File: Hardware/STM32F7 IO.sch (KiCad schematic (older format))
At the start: 28 parts, among them U16 STM32F765ZGT6

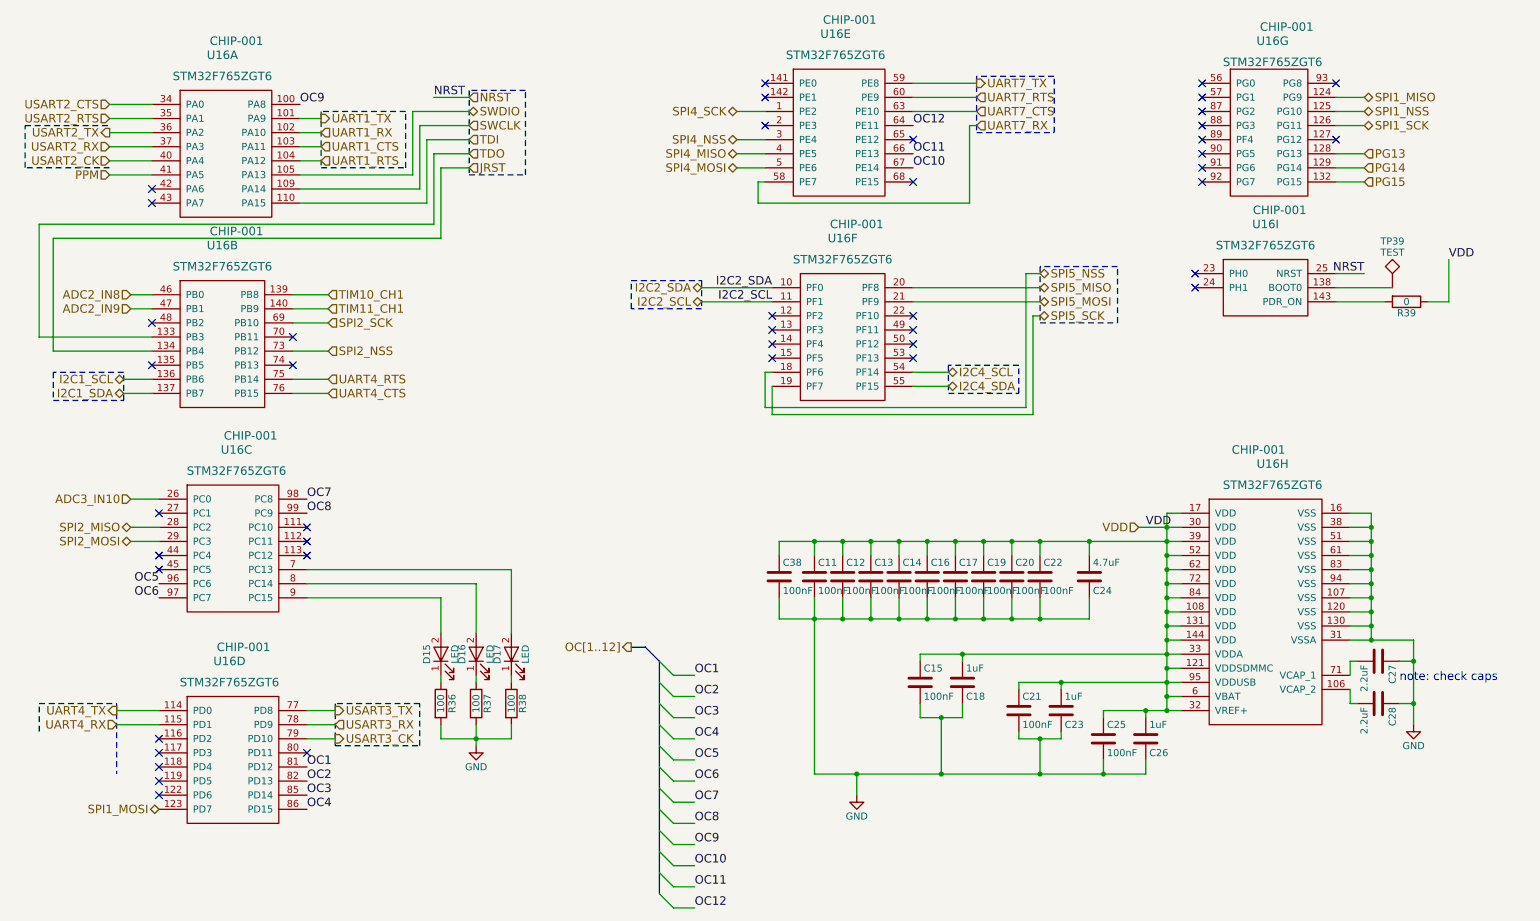
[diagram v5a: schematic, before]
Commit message: Restarted work
Removed OC and SEL busses. Still need to add clocks.
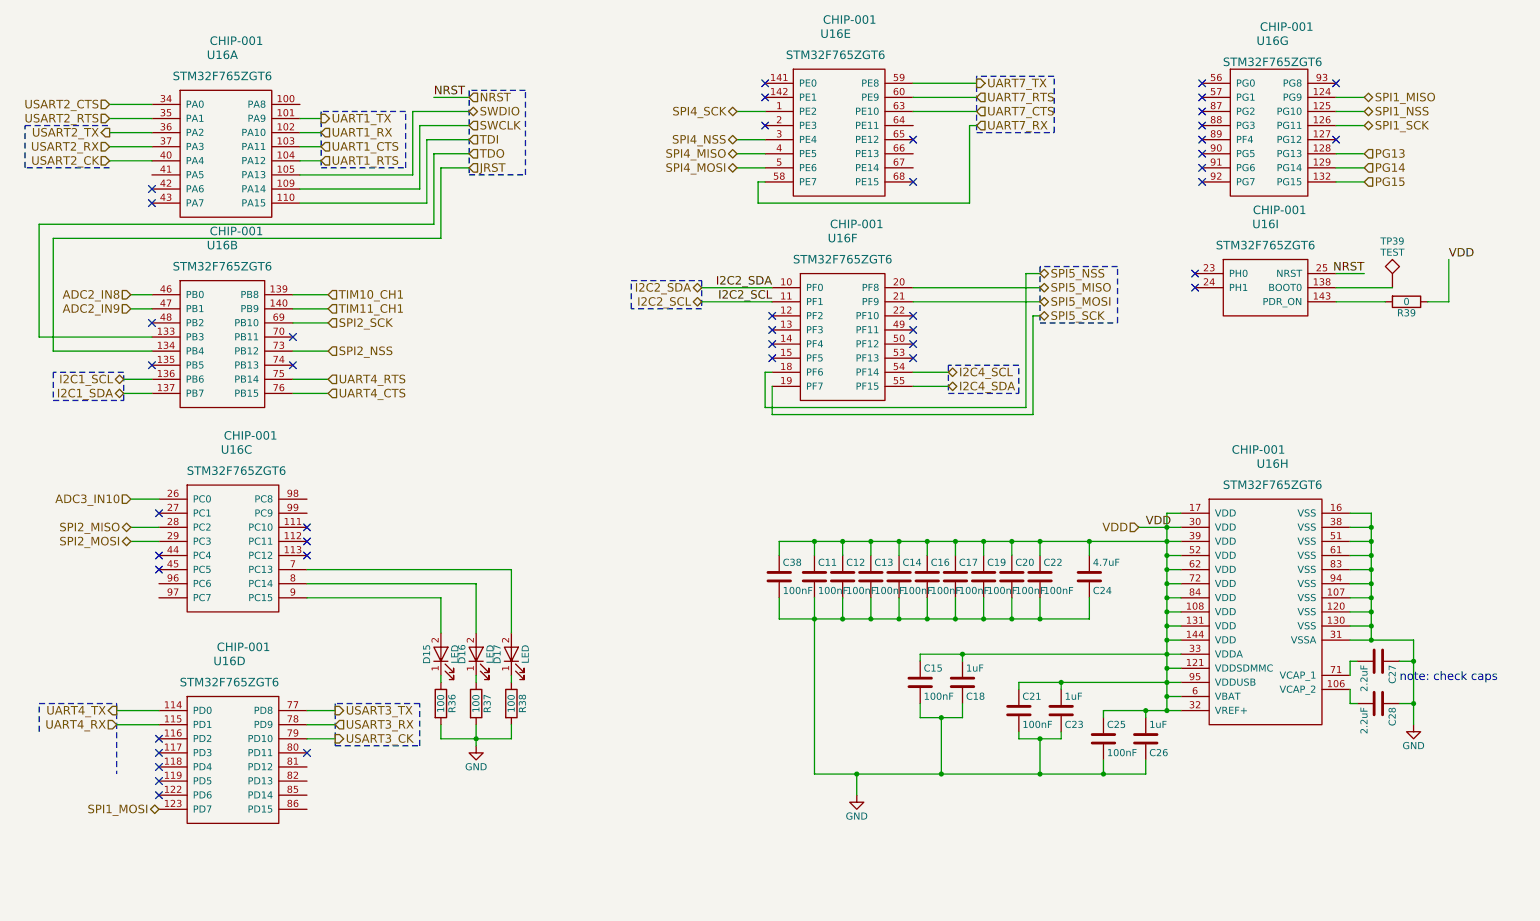
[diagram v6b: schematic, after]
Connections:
- net OC1: no longer names the net of U16.81 (PD12)
- net OC10: no longer names the net of U16.67 (PE14)
- net OC11: no longer names the net of U16.66 (PE13)
- net OC12: no longer names the net of U16.64 (PE11)
- net OC2: no longer names the net of U16.82 (PD13)
- net OC3: no longer names the net of U16.85 (PD14)
- net OC4: no longer names the net of U16.86 (PD15)
- net OC5: no longer names the net of U16.96 (PC6)
- net OC6: no longer names the net of U16.97 (PC7)
- net OC7: no longer names the net of U16.98 (PC8)
- net OC8: no longer names the net of U16.99 (PC9)
- net OC9: no longer names the net of U16.100 (PA8)
- net PPM: no longer names the net of U16.41 (PA5)
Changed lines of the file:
@@
 EESchema Schematic File Version 2
+LIBS:ZeroPilot-rescue
 LIBS:WARG
 LIBS:power
@@
 $Descr A4 11693 8268
 encoding utf-8
-Sheet 17 21
+Sheet 5 8
 Title "Autopilot Controller I/O"
 Date "2017-05-14"
@@
 Comment4 ""
 $EndDescr
-Text Label 2750 6300 0    60   ~ 0
-OC1
-Text Label 2750 6400 0    60   ~ 0
-OC2
-Text Label 2750 6500 0    60   ~ 0
-OC3
-Text Label 2750 6600 0    60   ~ 0
-OC4
-Text Label 1700 5000 2    60   ~ 0
-OC5
-Text Label 1700 5100 2    60   ~ 0
-OC6
-Text Label 2750 4400 0    60   ~ 0
-OC7
-Text Label 2700 1600 0    60   ~ 0
-OC9
-Text Label 7050 2050 0    60   ~ 0
-OC10
-Text Label 7050 1950 0    60   ~ 0
-OC11
-Text Label 7050 1750 0    60   ~ 0
-OC12
-Text HLabel 1350 2100 0    60   Input ~ 0
-PPM
-Text HLabel 5050 5450 0    60   Output ~ 0
-OC[1..12]
-Entry Wire Line
-	5250 5550 5350 5650
-Entry Wire Line
-	5250 5700 5350 5800
-Entry Wire Line
-	5250 5850 5350 5950
-Entry Wire Line
-	5250 6000 5350 6100
-Entry Wire Line
-	5250 6150 5350 6250
-Entry Wire Line
-	5250 6300 5350 6400
-Entry Wire Line
-	5250 6450 5350 6550
-Entry Wire Line
-	5250 6600 5350 6700
-Entry Wire Line
-	5250 6750 5350 6850
-Entry Wire Line
-	5250 6900 5350 7000
-Entry Wire Line
-	5250 7050 5350 7150
-Entry Wire Line
-	5250 7200 5350 7300
-Text Label 5500 7300 0    60   ~ 0
-OC12
-Text Label 5500 7150 0    60   ~ 0
-OC11
-Text Label 5500 7000 0    60   ~ 0
-OC10
-Text Label 5500 6850 0    60   ~ 0
-OC9
-Text Label 5500 6700 0    60   ~ 0
-OC8
-Text Label 5500 6550 0    60   ~ 0
-OC7
-Text Label 5500 6400 0    60   ~ 0
-OC6
-Text Label 5500 6250 0    60   ~ 0
-OC5
-Text Label 5500 6100 0    60   ~ 0
-OC4
-Text Label 5500 5950 0    60   ~ 0
-OC3
-Text Label 5500 5800 0    60   ~ 0
-OC2
-Text Label 5500 5650 0    60   ~ 0
-OC1
-Text Label 2750 4500 0    60   ~ 0
-OC8
 Text Label 10250 2800 2    60   ~ 0
 NRST
@@
 	7950 2800 7850 2800
 Wire Wire Line
-	1350 2100 1650 2100
-Wire Wire Line
 	2650 2950 2900 2950
 Wire Wire Line
@@
 Wire Wire Line
 	2700 2100 3500 2100
-Wire Wire Line
-	5350 7300 5500 7300
-Wire Wire Line
-	5350 7150 5500 7150
-Wire Wire Line
-	5350 7000 5500 7000
-Wire Wire Line
-	5350 6850 5500 6850
-Wire Wire Line
-	5350 6700 5500 6700
-Wire Wire Line
-	5350 6550 5500 6550
-Wire Wire Line
-	5350 6400 5500 6400
-Wire Wire Line
-	5350 6250 5500 6250
-Wire Wire Line
-	5350 6100 5500 6100
-Wire Wire Line
-	5350 5950 5500 5950
-Wire Wire Line
-	5500 5800 5350 5800
-Wire Wire Line
-	5500 5650 5350 5650
-Wire Bus Line
-	5250 5550 5250 7200
-Wire Bus Line
-	5150 5450 5250 5550
-Wire Bus Line
-	5050 5450 5150 5450
 Text HLabel 10250 2050 2    60   Input ~ 0
 PG14

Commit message: Added clock, cleaned up files
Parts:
- added C? (x2): 7pF, Resistors_SMD:R_0603_HandSoldering, symbol C
- added C? (x2): 14pF, Resistors_SMD:R_0603_HandSoldering, symbol C
- added Y?: 8MHz, Crystals:Crystal_SMD_5032-2pin_5.0x3.2mm_HandSoldering, symbol Crystal
- added Y?: 32.768kHz, Crystals:Crystal_SMD_MicroCrystal_CC7V-T1A-2pin_3.2x1.5mm_HandSoldering, symbol Crystal
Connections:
- net GND: now also C?.2, C?.2
- net at D16.2 (A): now also U16.112 (PC11); no longer U16.8 (PC14)
- net at D17.2 (A): now also U16.111 (PC10); no longer U16.7 (PC13)
- net at D15.2 (A): now also U16.113 (PC12); no longer U16.9 (PC15)
- net at U16.23 (PH0): now also C?.1, Y?.1
- net at U16.24 (PH1): now also C?.1, Y?.2
- new net: C?.1, U16.8 (PC14), Y?.2
- new net: C?.1, U16.9 (PC15), Y?.1
- new net: C?.2, C?.2
- no-connect marks 43 -> 38
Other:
- note removed: "note: check caps\n"
- moved on the sheet: D15, D16, D17, R36, R37, R38

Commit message: Placement and preminiary routing
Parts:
- gave numbers to parts that had none: 6
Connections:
- net UART7_CTS: no longer names the net of U16.63 (PE10)
- net UART7_RTS: no longer names the net of U16.60 (PE9)
- net UART7_RX: no longer names the net of U16.58 (PE7)
- net UART7_TX: no longer names the net of U16.59 (PE8)
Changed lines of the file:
@@
 Text HLabel 7300 3600 2    60   BiDi ~ 0
 I2C4_SDA
-Text HLabel 7500 1450 2    60   Output ~ 0
-UART7_TX
-Text HLabel 7500 1750 2    60   Input ~ 0
-UART7_RX
 Text HLabel 2850 1800 2    60   Input ~ 0
 UART1_RX
@@
 $EndComp
 $Comp
-L GND #PWR046
+L GND #PWR27
 U 1 1 591E59BE
 P 10600 6000
-F 0 "#PWR046" H 10600 5750 50  0001 C CNN
+F 0 "#PWR27" H 10600 5750 50  0001 C CNN
 F 1 "GND" H 10600 5850 50  0000 C CNN
 F 2 "" H 10600 6000 50  0001 C CNN
@@
 $EndComp
 $Comp
-L GND #PWR047
+L GND #PWR25
 U 1 1 591EB43A
 P 6650 6500
-F 0 "#PWR047" H 6650 6250 50  0001 C CNN
+F 0 "#PWR25" H 6650 6250 50  0001 C CNN
 F 1 "GND" H 6650 6350 50  0000 C CNN
 F 2 "" H 6650 6500 50  0001 C CNN
@@
 Text HLabel 2900 3650 2    60   Input ~ 0
 UART4_CTS
-Text HLabel 7500 1650 2    60   Input ~ 0
-UART7_CTS
-Text HLabel 7500 1550 2    60   Input ~ 0
-UART7_RTS
 Text HLabel 2900 3150 2    60   Input ~ 0
 SPI2_SCK
@@
 Wire Wire Line
 	2950 6100 2750 6100
-Wire Notes Line
-	8050 1400 7500 1400
-Wire Notes Line
-	8050 1800 8050 1400
-Wire Notes Line
-	7500 1800 8050 1800
-Wire Notes Line
-	7500 1400 7500 1800
-Wire Wire Line
-	7450 1750 7500 1750
-Wire Wire Line
-	5950 2150 5950 2300
-Wire Wire Line
-	6000 2150 5950 2150
 Wire Wire Line
 	7850 3100 7950 3100
@@
 	0    -1   -1   0
 $EndComp
-Wire Wire Line
-	5950 2300 7450 2300
-Wire Wire Line
-	7450 2300 7450 1750
-Wire Wire Line
-	7500 1650 7050 1650
-Wire Wire Line
-	7050 1550 7500 1550
-Wire Wire Line
-	7500 1450 7050 1450
 $Comp
 L R R36
@@
 Connection ~ 4400 5750
 $Comp
-L GND #PWR048
+L GND #PWR24
 U 1 1 59530E80
 P 4400 5800
-F 0 "#PWR048" H 4400 5550 50  0001 C CNN
+F 0 "#PWR24" H 4400 5550 50  0001 C CNN
 F 1 "GND" H 4400 5650 50  0000 C CNN
 F 2 "" H 4400 5800 50  0001 C CNN
@@
 	5950 3600 5950 3800
 $Comp
-L Crystal Y?
+L Crystal Y4
 U 1 1 5990B6F8
 P 8750 2850
-F 0 "Y?" H 8750 3000 50  0000 C CNN
+F 0 "Y4" H 8750 3000 50  0000 C CNN
 F 1 "8MHz" H 8750 2700 50  0000 C CNN
 F 2 "Crystals:Crystal_SMD_5032-2pin_5.0x3.2mm_HandSoldering" H 8750 2850 50  0001 C CNN
@@
 	9050 3000 9050 2900
 $Comp
-L C C?
+L C C42
 U 1 1 5990C3CD
 P 9000 3200
-F 0 "C?" H 9025 3300 50  0000 L CNN
+F 0 "C42" H 9025 3300 50  0000 L CNN
 F 1 "7pF" H 9025 3100 50  0000 L CNN
 F 2 "Resistors_SMD:R_0603_HandSoldering" H 9038 3050 50  0001 C CNN
@@
 $EndComp
 $Comp
-L C C?
+L C C41
 U 1 1 5990C3D5
 P 8800 3200
-F 0 "C?" H 8825 3300 50  0000 L CNN
+F 0 "C41" H 8825 3300 50  0000 L CNN
 F 1 "7pF" H 8825 3100 50  0000 L CNN
 F 2 "Resistors_SMD:R_0603_HandSoldering" H 8838 3050 50  0001 C CNN
@@
 Connection ~ 9000 2700
 $Comp
-L GND #PWR?
+L GND #PWR26
 U 1 1 5990C849
 P 8900 3500
-F 0 "#PWR?" H 8900 3250 50  0001 C CNN
+F 0 "#PWR26" H 8900 3250 50  0001 C CNN
 F 1 "GND" H 8900 3350 50  0000 C CNN
 F 2 "" H 8900 3500 50  0001 C CNN
@@
 	4150 4800 4150 5000
 $Comp
-L Crystal Y?
+L Crystal Y3
 U 1 1 5990E0A0
 P 3500 5050
-F 0 "Y?" H 3500 5200 50  0000 C CNN
+F 0 "Y3" H 3500 5200 50  0000 C CNN
 F 1 "32.768kHz" H 3500 4900 50  0000 C CNN
 F 2 "Crystals:Crystal_SMD_MicroCrystal_CC7V-T1A-2pin_3.2x1.5mm_HandSoldering" H 3500 5050 50  0001 C CNN
@@
 $EndComp
 $Comp
-L C C?
+L C C40
 U 1 1 5990E0AA
 P 3050 5450
-F 0 "C?" H 3075 5550 50  0000 L CNN
+F 0 "C40" H 3075 5550 50  0000 L CNN
 F 1 "14pF" H 3075 5350 50  0000 L CNN
 F 2 "Resistors_SMD:R_0603_HandSoldering" H 3088 5300 50  0001 C CNN
@@
 $EndComp
 $Comp
-L C C?
+L C C39
 U 1 1 5990E0B2
 P 2850 5450
-F 0 "C?" H 2875 5550 50  0000 L CNN
+F 0 "C39" H 2875 5550 50  0000 L CNN
 F 1 "14pF" H 2875 5350 50  0000 L CNN
 F 2 "Resistors_SMD:R_0603_HandSoldering" H 2888 5300 50  0001 C CNN
@@
 	3050 5700 3050 5600
 $Comp
-L GND #PWR?
+L GND #PWR23
 U 1 1 5990E97D
 P 2950 5700
-F 0 "#PWR?" H 2950 5450 50  0001 C CNN
+F 0 "#PWR23" H 2950 5450 50  0001 C CNN
 F 1 "GND" H 2950 5550 50  0000 C CNN
 F 2 "" H 2950 5700 50  0001 C CNN
